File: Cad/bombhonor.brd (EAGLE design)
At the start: 80 x 67.4 mm, 82 parts, among them U1 STM32L011F4P6

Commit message: Messa a posto la bom, creato excel e stime di costo
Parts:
- LED1, LED10, LED11, LED12, LED13, LED14, LED15, LED16, LED17, LED18, LED19, LED2, LED20, LED21, LED22, LED23, LED24, LED25, LED26, LED27, LED28, LED29, LED3, LED30, LED4, LED5, LED6, LED7, LED8, LED9: value RED -> BLUE

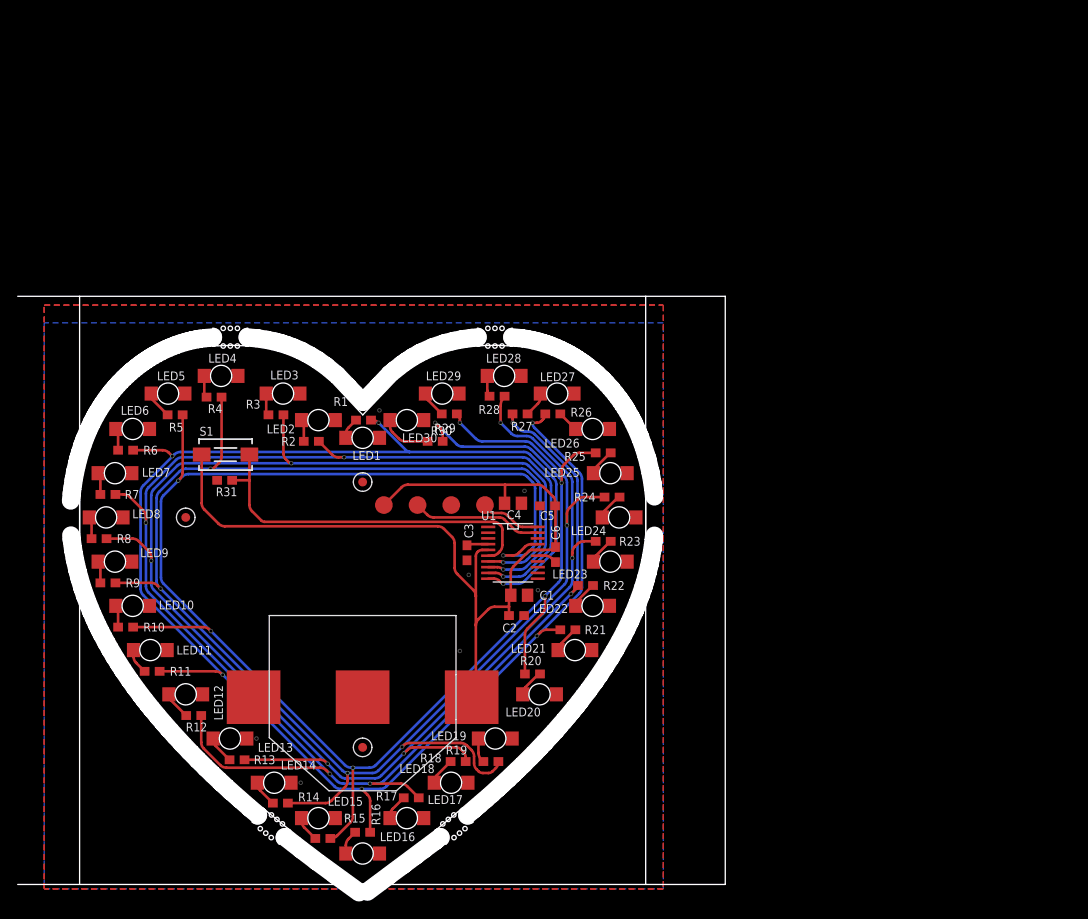
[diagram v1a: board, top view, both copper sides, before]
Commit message: Ultimato PCB, si procede con il pannello
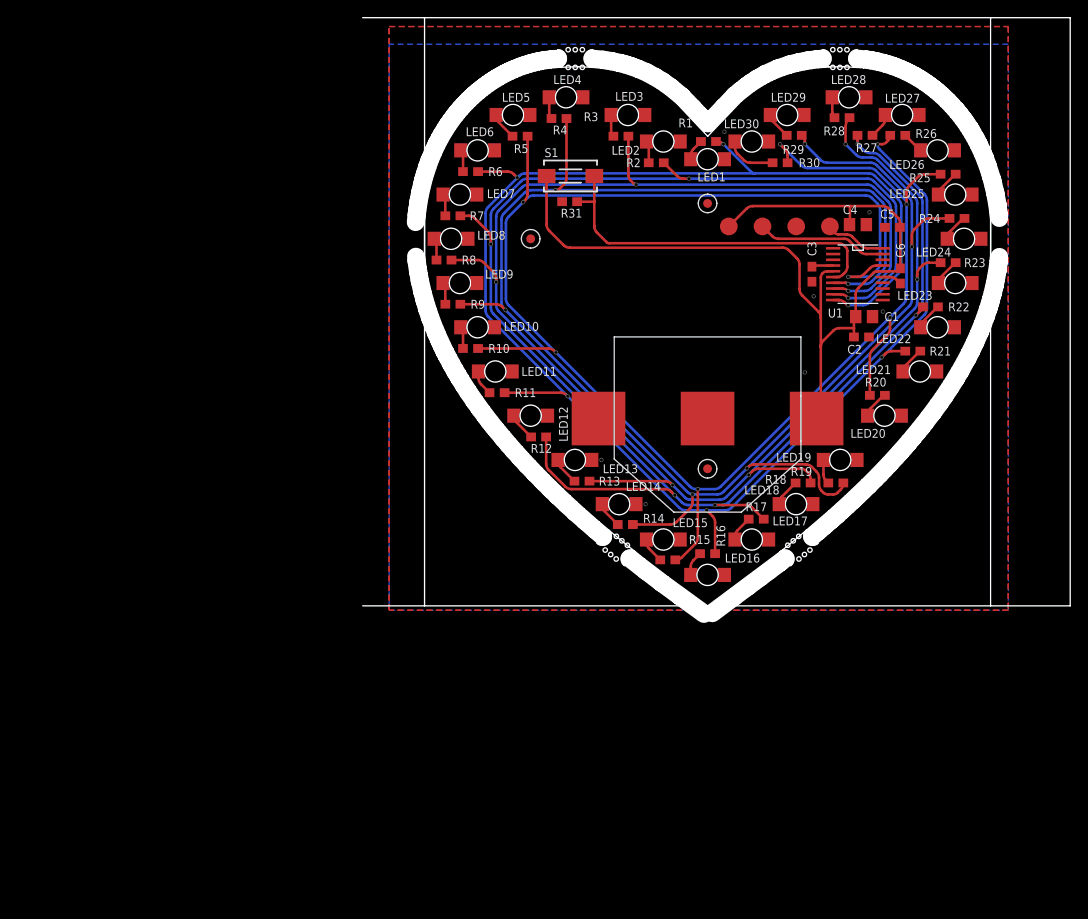
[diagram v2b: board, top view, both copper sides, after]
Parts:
- moved C1 50.1 mm to (56.7, 32.7)
- moved R26 50.1 mm to (60.5, 53.2)
- moved R27 50.1 mm to (56.8, 53.2)
- moved R28 50.1 mm to (54.2, 55.2)
- moved R29 50.1 mm to (48.8, 53.2)
- moved R31 50.1 mm to (23.4, 45.7)
- moved 1 50.1 mm to (24.0, 61.9)
- moved 2 50.1 mm to (54.0, 61.9)
- moved BATT1 50.1 mm to (39.0, 20.5)
- moved C2 50.1 mm to (56.4, 30.4)
- moved C3 50.1 mm to (50.8, 37.5)
- moved C4 50.1 mm to (56.0, 43.1)
- moved C5 50.1 mm to (59.9, 42.8)
- moved C6 50.1 mm to (60.8, 37.3)
- moved LED1 50.1 mm to (39.0, 50.5)
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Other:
- outline, holes or cut-outs redrawn

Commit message: Pannellizzato ogni cosa
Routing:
- net GND: track 2.24 -> 13.9 mm, vias 8 -> 10
- net +3V3: track 105.4 -> 104.7 mm
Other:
- board text added: "C1"
- board text added: "C2"
- board text added: "C3"
- board text added: "C4"
- board text added: "C5"
- board text added: "C6"
- board text added: "LED1"
- board text added: "LED10"
- board text added: "LED11"
- board text added: "LED12"
- board text added: "LED13"
- board text added: "LED14"
- board text added: "LED15"
- board text added: "LED16"
- board text added: "LED17"
- board text added: "LED18"
- board text added: "LED19"
- board text added: "LED2"
- board text added: "LED20"
- board text added: "LED21"
- board text added: "LED22"
- board text added: "LED23"
- board text added: "LED24"
- board text added: "LED25"
- board text added: "LED26"
- board text added: "LED27"
- board text added: "LED28"
- board text added: "LED29"
- board text added: "LED3"
- board text added: "LED30"
- board text added: "LED4"
- board text added: "LED5"
- board text added: "LED6"
- board text added: "LED7"
- board text added: "LED8"
- board text added: "LED9"
- board text added: "R1"
- board text added: "R10"
- board text added: "R11"
- board text added: "R12"
- board text added: "R13"
- board text added: "R14"
- board text added: "R15"
- board text added: "R16"
- board text added: "R17"
- board text added: "R18"
- board text added: "R19"
- board text added: "R2"
- board text added: "R20"
- board text added: "R21"
- board text added: "R22"
- board text added: "R23"
- board text added: "R24"
- board text added: "R25"
- board text added: "R26"
- board text added: "R27"
- board text added: "R28"
- board text added: "R29"
- board text added: "R3"
- board text added: "R30"
- board text added: "R31"
- board text added: "R4"
- board text added: "R5"
- board text added: "R6"
- board text added: "R7"
- board text added: "R8"
- board text added: "R9"
- board text added: "S1"
- board text added: "U1"
